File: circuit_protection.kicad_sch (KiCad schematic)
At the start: 37 parts, among them IC2 TPS26632RGET, Q5 2N7002, Q6 CSD19537Q3, U10 USBLC6-2SC6, U11 USBLC6-2SC6, U2 SEUC10F5V4U, U3 TPS259630DDAR, U8 USBLC6-2SC6

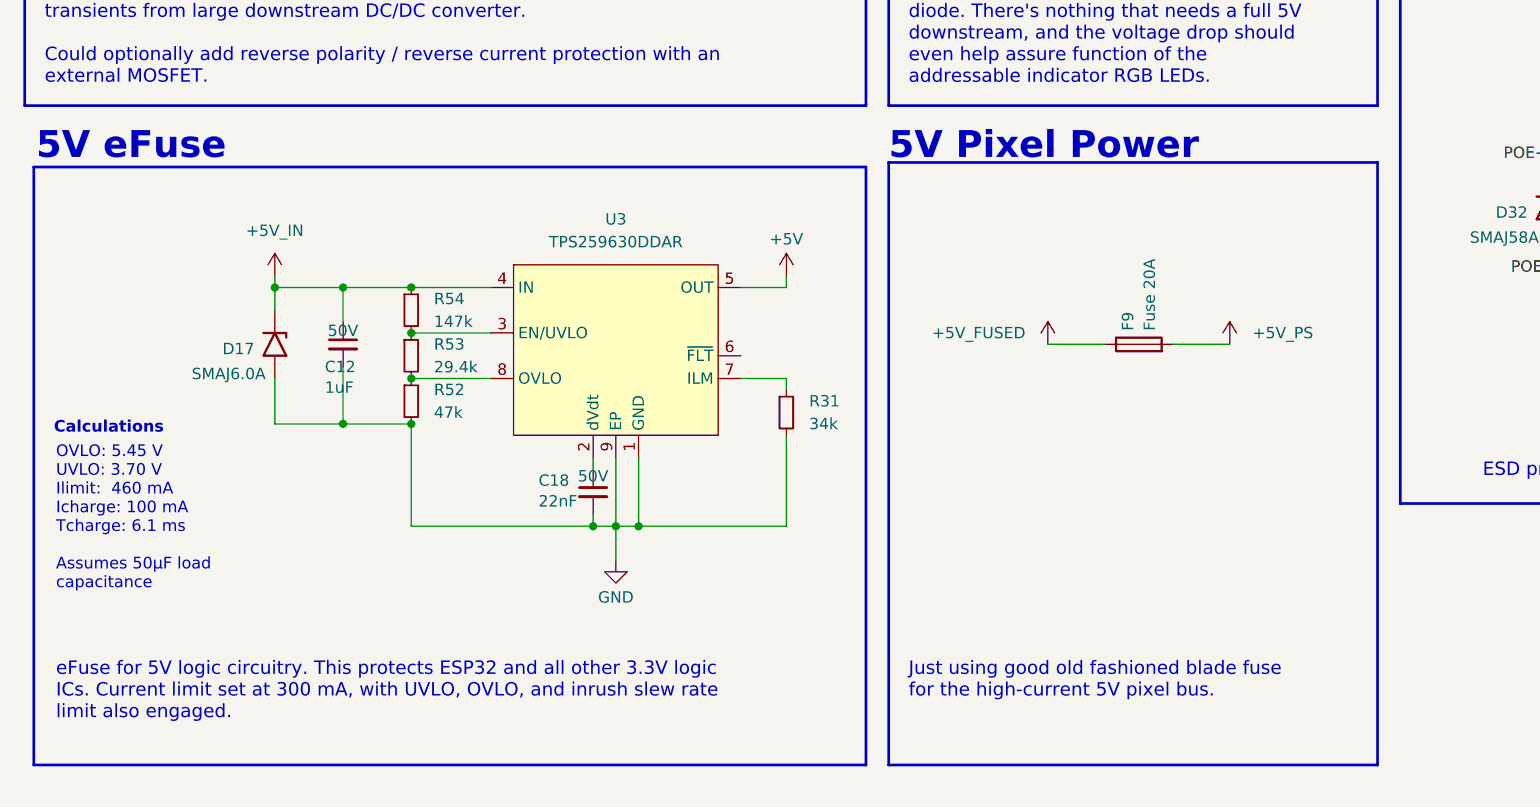
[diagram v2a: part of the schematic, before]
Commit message: added 5V input ideal diode reverse polarity protection
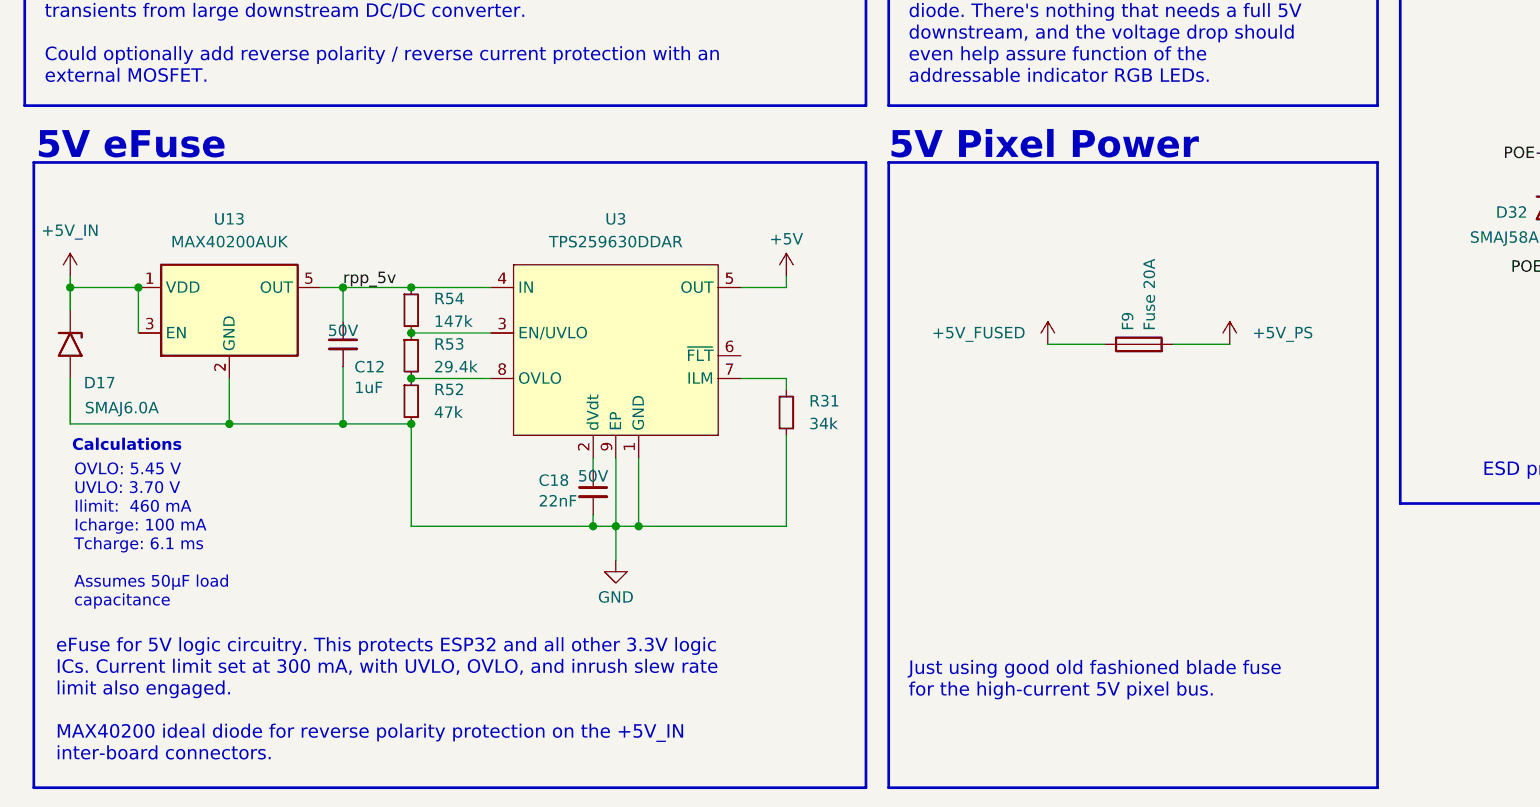
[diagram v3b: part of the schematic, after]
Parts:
- added U13: MAX40200AUK, Package_TO_SOT_SMD:SOT-23-5, symbol Analog_Switch:MAX40200AUK
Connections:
- net +5V_IN: now also U13.1 (VDD), U13.3 (EN); no longer C12.1, R54.1, U3.4 (IN)
- net GND: now also U13.2 (GND)
- new net rpp_5v: C12.1, R54.1, U13.5 (OUT), U3.4 (IN)
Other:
- moved on the sheet: D17
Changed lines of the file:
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@@
 	)
 	(rectangle
-		(start 21.336 126.238)
-		(end 114.3 193.04)
+		(start 21.336 125.73)
+		(end 114.3 195.58)
 		(stroke
 			(width 0.3)
@@
 	(rectangle
 		(start 116.84 125.73)
-		(end 171.45 193.04)
+		(end 171.45 195.58)
 		(stroke
 			(width 0.3)
@@
 	(text "Calculations"
 		(exclude_from_sim no)
-		(at 29.718 155.448 0)
+		(at 31.75 157.48 0)
 		(effects
 			(font
@@
 		)
 	)
-	(text_box "eFuse for 5V logic circuitry. This protects ESP32 and all other 3.3V logic ICs. Current limit set at 300 mA, with UVLO, OVLO, and inrush slew rate limit also engaged. \n"
+	(text_box "eFuse for 5V logic circuitry. This protects ESP32 and all other 3.3V logic ICs. Current limit set at 300 mA, with UVLO, OVLO, and inrush slew rate limit also engaged. \n\nMAX40200 ideal diode for reverse polarity protection on the +5V_IN inter-board connectors."
 		(exclude_from_sim no)
-		(at 22.86 180.34 0)
+		(at 22.86 177.8 0)
 		(size 91.44 12.065)
 		(margins 0.9525 0.9525 0.9525 0.9525)
@@
 	(text_box "OVLO: 5.45 V\nUVLO: 3.70 V\nIlimit:  460 mA\nIcharge: 100 mA\nTcharge: 6.1 ms\n\nAssumes 50µF load capacitance"
 		(exclude_from_sim no)
-		(at 22.86 156.21 0)
-		(size 31.75 22.86)
+		(at 24.892 158.242 0)
+		(size 31.75 18.288)
 		(margins 0.9525 0.9525 0.9525 0.9525)
 		(stroke
@@
 	)
 	(junction
+		(at 33.02 139.7)
+		(diameter 0)
+		(color 0 0 0 0)
+	)
+	(junction
 		(at 76.2 85.09)
 		(diameter 0)
@@
 	)
 	(junction
-		(at 48.26 139.7)
+		(at 25.4 139.7)
 		(diameter 0)
 		(color 0 0 0 0)
@@
 	)
 	(junction
+		(at 43.18 154.94)
+		(diameter 0)
+		(color 0 0 0 0)
+	)
+	(junction
 		(at 52.07 63.5)
 		(diameter 0)
@@
 	(wire
 		(pts
+			(xy 43.18 154.94) (xy 55.88 154.94)
+		)
+		(stroke
+			(width 0)
+			(type default)
+		)
+	)
+	(wire
+		(pts
 			(xy 55.88 148.59) (xy 55.88 154.94)
 		)
@@
 	(wire
 		(pts
-			(xy 48.26 139.7) (xy 55.88 139.7)
+			(xy 25.4 139.7) (xy 33.02 139.7)
 		)
 		(stroke
@@
 		)
 	)
+	(wire
+		(pts
+			(xy 43.18 149.86) (xy 43.18 154.94)
+		)
+		(stroke
+			(width 0)
+			(type default)
+		)
+	)
 	(bus
 		(pts
@@
 	(wire
 		(pts
+			(xy 53.34 139.7) (xy 55.88 139.7)
+		)
+		(stroke
+			(width 0)
+			(type default)
+		)
+	)
+	(wire
+		(pts
 			(xy 195.58 93.98) (xy 205.74 93.98)
 		)
@@
 	(wire
 		(pts
-			(xy 48.26 154.94) (xy 55.88 154.94)
+			(xy 25.4 154.94) (xy 43.18 154.94)
 		)
 		(stroke
@@
 	(wire
 		(pts
-			(xy 48.26 138.43) (xy 48.26 139.7)
+			(xy 25.4 138.43) (xy 25.4 139.7)
 		)
 		(stroke
@@
 	(wire
 		(pts
-			(xy 48.26 149.86) (xy 48.26 154.94)
+			(xy 25.4 149.86) (xy 25.4 154.94)
 		)
 		(stroke
@@
 	(wire
 		(pts
+			(xy 33.02 139.7) (xy 33.02 144.78)
+		)
+		(stroke
+			(width 0)
+			(type default)
+		)
+	)
+	(wire
+		(pts
 			(xy 63.5 149.86) (xy 72.39 149.86)
 		)
@@
 	(wire
 		(pts
-			(xy 48.26 142.24) (xy 48.26 139.7)
+			(xy 25.4 142.24) (xy 25.4 139.7)
 		)
 		(stroke
@@
 		)
 	)
+	(label "rpp_5v"
+		(at 55.88 139.7 0)
+		(effects
+			(font
+				(size 1.27 1.27)
+			)
+			(justify left bottom)
+		)
+	)
 	(label "SCL_ESP"
 		(at 241.3 59.69 0)
@@
 	)
 	(symbol
+		(lib_id "Analog_Switch:MAX40200AUK")
+		(at 43.18 142.24 0)
+		(unit 1)
+		(exclude_from_sim no)
+		(in_bom yes)
+		(on_board yes)
+		(dnp no)
+		(fields_autoplaced yes)
+		(property "Reference" "U13"
+			(at 43.18 132.08 0)
+			(effects
+				(font
+					(size 1.27 1.27)
+				)
+			)
+		)
+		(property "Value" "MAX40200AUK"
+			(at 43.18 134.62 0)
+			(effects
+				(font
+					(size 1.27 1.27)
+				)
+			)
+		)
+		(property "Footprint" "Package_TO_SOT_SMD:SOT-23-5"
+			(at 43.18 129.54 0)
+			(effects
+				(font
+					(size 1.27 1.27)
+				)
+				(hide yes)
+			)
+		)
+		(property "Datasheet" "https://datasheets.maximintegrated.com/en/ds/MAX40200.pdf"
+			(at 43.18 129.54 0)
+			(effects
+				(font
+					(size 1.27 1.27)
+				)
+				(hide yes)
+			)
+		)
+		(property "Description" "Ideal Diode, Ultra-Low Voltage Drop, 1.5-5.5V, 1A, SOT-23-5"
+			(at 43.18 142.24 0)
+			(effects
+				(font
+					(size 1.27 1.27)
+				)
+				(hide yes)
+			)
+		)
+		(pin "2"
+		)
+		(pin "4"
+		)
+		(pin "3"
+		)
+		(pin "5"
+		)
+		(pin "1"
+		)
+		(instances
+			(project ""
+				(path "/bf4b09fd-2d42-43b2-9834-c05987d36a77/699e3cd3-5536-411e-b1c2-d359c75a8476"
+					(reference "U13")
+					(unit 1)
+				)
+			)
+		)
+	)
+	(symbol
 		(lib_id "Device:R_Small")
 		(at 52.07 68.58 0)
@@
 	(symbol
 		(lib_id "power:+24V")
-		(at 48.26 138.43 0)
+		(at 25.4 138.43 0)
 		(unit 1)
 		(exclude_from_sim no)
@@
 		(fields_autoplaced yes)
 		(property "Reference" "#PWR0133"
-			(at 48.26 142.24 0)
+			(at 25.4 142.24 0)
 			(effects
 				(font
@@
 		)
 		(property "Value" "+5V_IN"
-			(at 48.26 133.35 0)
+			(at 25.4 133.35 0)
 			(effects
 				(font
@@
 		)
 		(property "Footprint" ""
-			(at 48.26 138.43 0)
+			(at 25.4 138.43 0)
 			(effects
 				(font
@@
 		)
 		(property "Datasheet" ""
-			(at 48.26 138.43 0)
+			(at 25.4 138.43 0)
 			(effects
 				(font
@@
 		)
 		(property "Description" "Power symbol creates a global label with name \"+24V\""
-			(at 48.26 138.43 0)
+			(at 25.4 138.43 0)
 			(effects
 				(font
@@
 		)
 		(property "LCSC" ""
-			(at 48.26 138.43 0)
+			(at 25.4 138.43 0)
 			(effects
 				(font
@@
 	(symbol
 		(lib_id "Diode:SMAJ24A")
-		(at 48.26 146.05 270)
+		(at 25.4 146.05 270)
 		(unit 1)
 		(exclude_from_sim no)
@@
 		(dnp no)
 		(property "Reference" "D17"
-			(at 45.974 146.558 90)
+			(at 30.48 150.368 90)
 			(effects
 				(font
@@
 		)
 		(property "Value" "SMAJ6.0A"
-			(at 47.244 149.352 90)
+			(at 35.306 153.162 90)
 			(effects
 				(font
@@
 		)
 		(property "Footprint" "Diode_SMD:D_SMA"
-			(at 43.18 146.05 0)
+			(at 20.32 146.05 0)
 			(effects
 				(font
@@
 		)
 		(property "Datasheet" "https://www.littelfuse.com/media?resourcetype=datasheets&itemid=75e32973-b177-4ee3-a0ff-cedaf1abdb93&filename=smaj-datasheet"
-			(at 48.26 144.78 0)
+			(at 25.4 144.78 0)
 			(effects
 				(font
@@
 		)
 		(property "Description" "400W unidirectional Transient Voltage Suppressor, 24.0Vr, SMA(DO-214AC)"
-			(at 48.26 146.05 0)
+			(at 25.4 146.05 0)
 			(effects
 				(font
@@
 		)
 		(property "LCSC" "C80275"
-			(at 48.26 146.05 0)
+			(at 25.4 146.05 0)
 			(effects
 				(font
@@
 		)
 		(property "color" ""
-			(at 48.26 146.05 0)
+			(at 25.4 146.05 0)
 			(effects
 				(font
@@
 		)
 		(property "Rating" ""
-			(at 48.26 146.05 0)
+			(at 25.4 146.05 0)
 			(effects
 				(font
@@
 		(dnp no)
 		(property "Reference" "C12"
-			(at 53.848 148.5646 0)
+			(at 57.15 148.59 0)
 			(effects
 				(font
@@
 		)
 		(property "Value" "1uF"
-			(at 53.848 150.876 0)
+			(at 57.15 150.9014 0)
 			(effects
 				(font

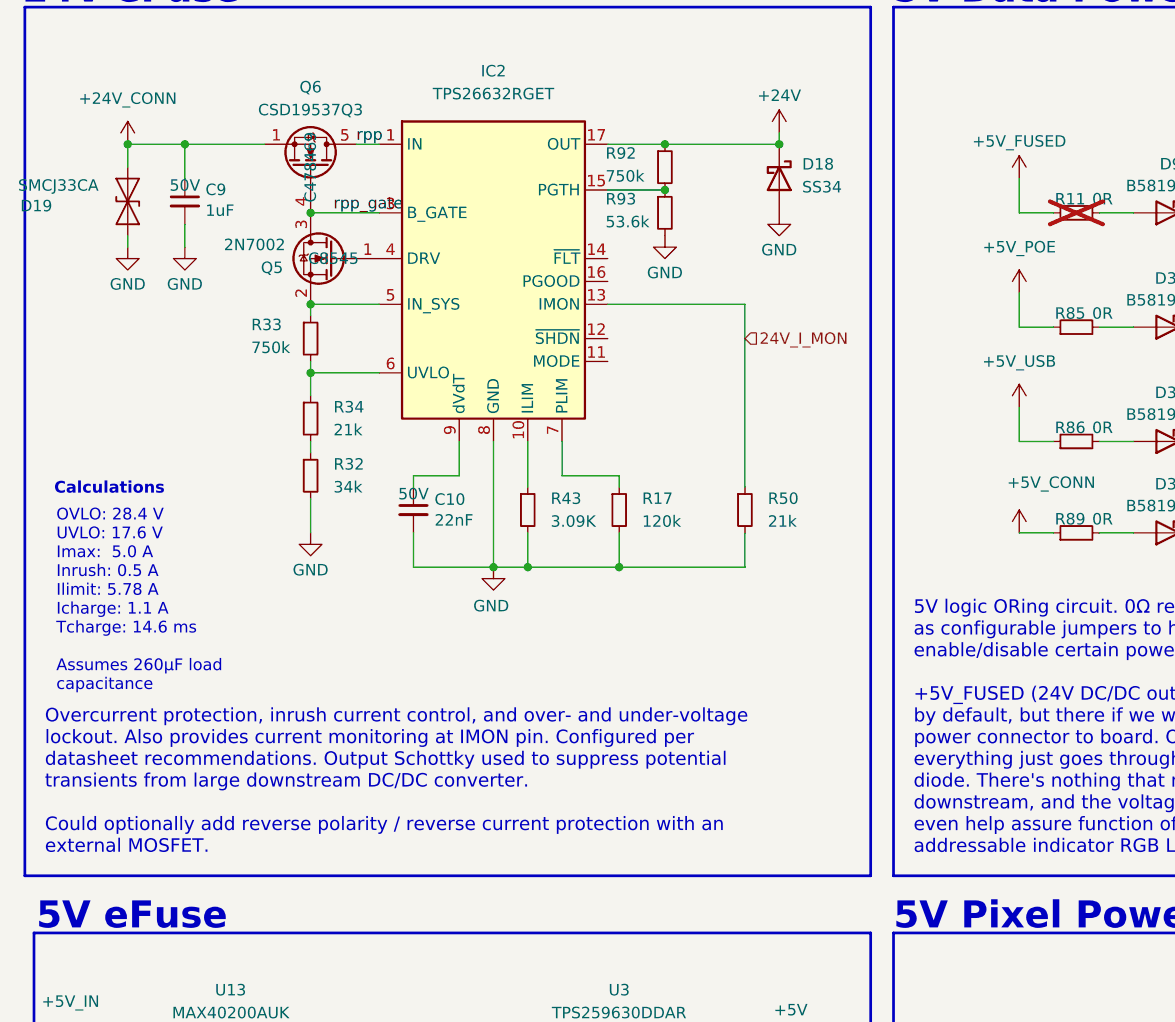
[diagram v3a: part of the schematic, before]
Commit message: made compatible with different 24V eFuse SKUs
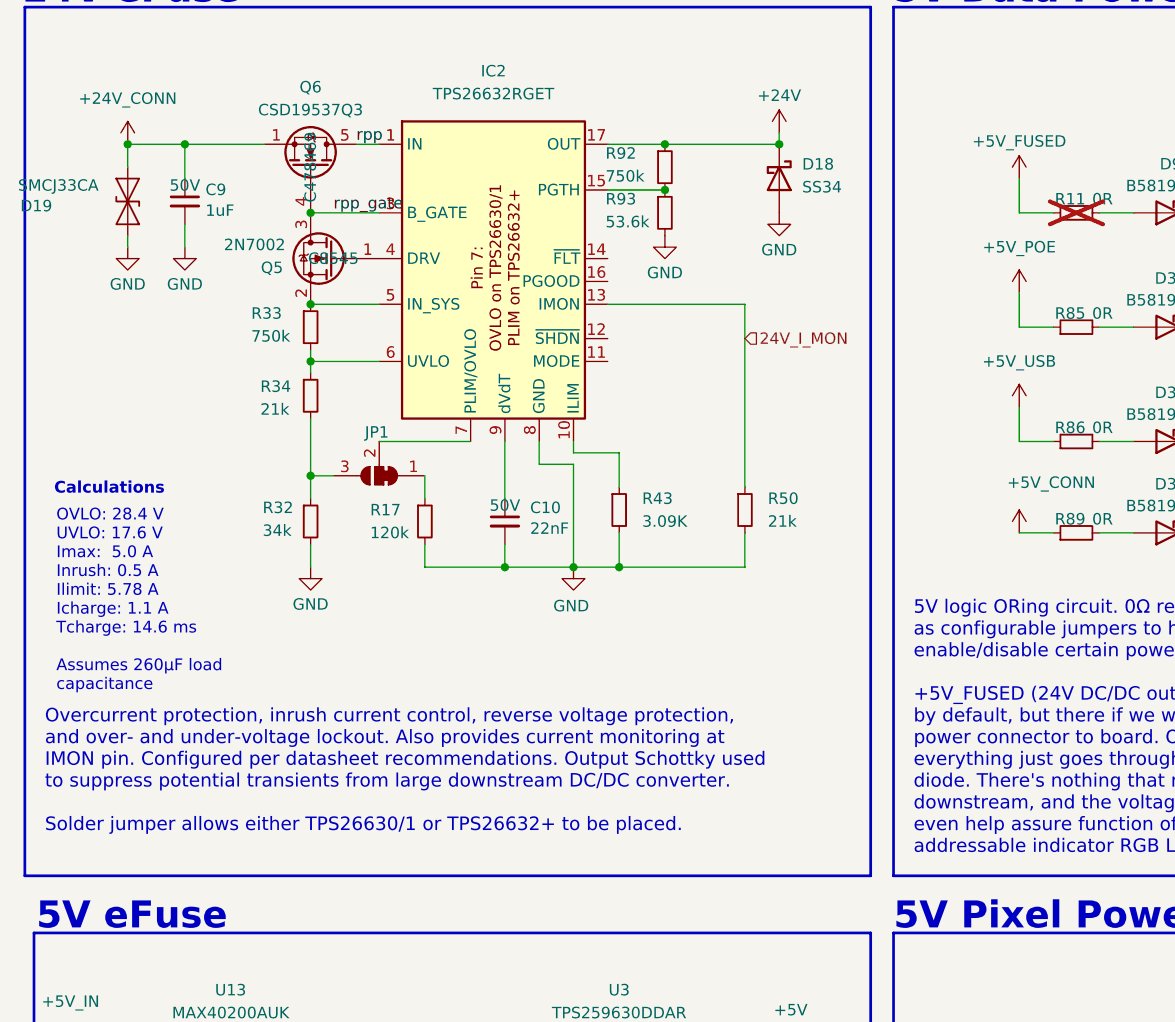
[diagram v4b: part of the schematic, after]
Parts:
- added JP1: SolderJumper_3_Bridged12, Jumper:SolderJumper-3_P1.3mm_Bridged12_RoundedPad1.0x1.5mm, symbol Jumper:SolderJumper_3_Bridged12
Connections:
- net GND: no longer IC2.25 (GND)
- net at R32.1, R34.2: now also JP1.3 (B)
- net at R17.1: now also JP1.1 (A); no longer IC2.7 (PLIM)
- new net: IC2.7 (PLIM/OVLO), JP1.2 (C)
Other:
- moved on the sheet: C10, R17, R32, R33, R34, R43

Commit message: MOAR STITCHING and some cleanup
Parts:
- D19: footprint Diode_SMD:D_SMA -> Diode_SMD:D_SMC; symbol Diode:SMAJ5.0CA -> Device:D_TVS
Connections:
- net GND: now also IC2.25 (PAD)
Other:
- moved on the sheet: C10, JP1, R17, R32

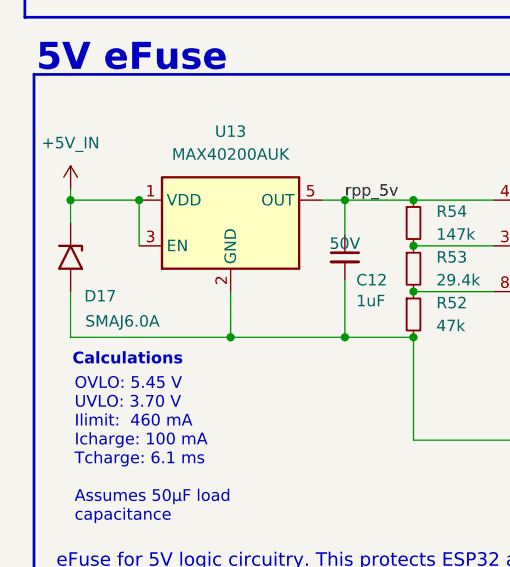
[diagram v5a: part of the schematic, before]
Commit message: added power diagram
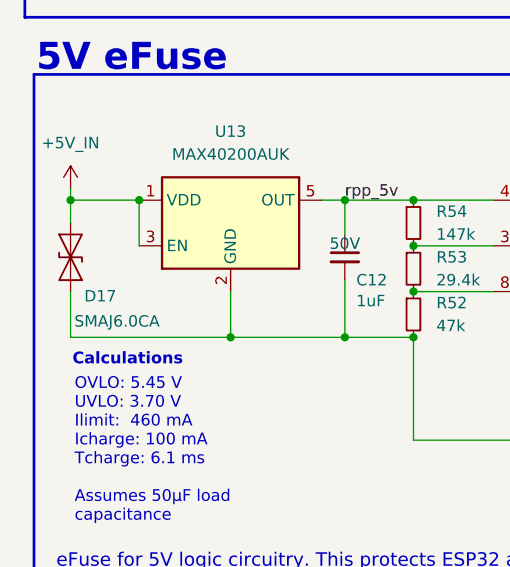
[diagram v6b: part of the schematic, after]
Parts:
- D17: value SMAJ6.0A -> SMAJ6.0CA; symbol Diode:SMAJ24A -> Diode:SMAJ6.0CA
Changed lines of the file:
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@@
 	)
 	(symbol
-		(lib_id "Diode:SMAJ24A")
+		(lib_id "Diode:SMAJ6.0CA")
 		(at 25.4 146.05 270)
 		(unit 1)
@@
 			)
 		)
-		(property "Value" "SMAJ6.0A"
+		(property "Value" "SMAJ6.0CA"
 			(at 35.306 153.162 90)
 			(effects
@@
 		)
 		(property "Datasheet" "https://www.littelfuse.com/media?resourcetype=datasheets&itemid=75e32973-b177-4ee3-a0ff-cedaf1abdb93&filename=smaj-datasheet"
-			(at 25.4 144.78 0)
+			(at 25.4 146.05 0)
 			(effects
 				(font
@@
 			)
 		)
-		(property "Description" "400W unidirectional Transient Voltage Suppressor, 24.0Vr, SMA(DO-214AC)"
+		(property "Description" "400W bidirectional Transient Voltage Suppressor, 6.0Vr, SMA(DO-214AC)"
 			(at 25.4 146.05 0)
 			(effects
